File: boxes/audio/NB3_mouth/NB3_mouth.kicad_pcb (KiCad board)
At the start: 2 copper layers, 20 x 18 mm, 4 parts, among them IC1 MAX98357AETE+T, J1 Conn_02x03_Odd_Even, J2 Conn_02x03_Odd_Even

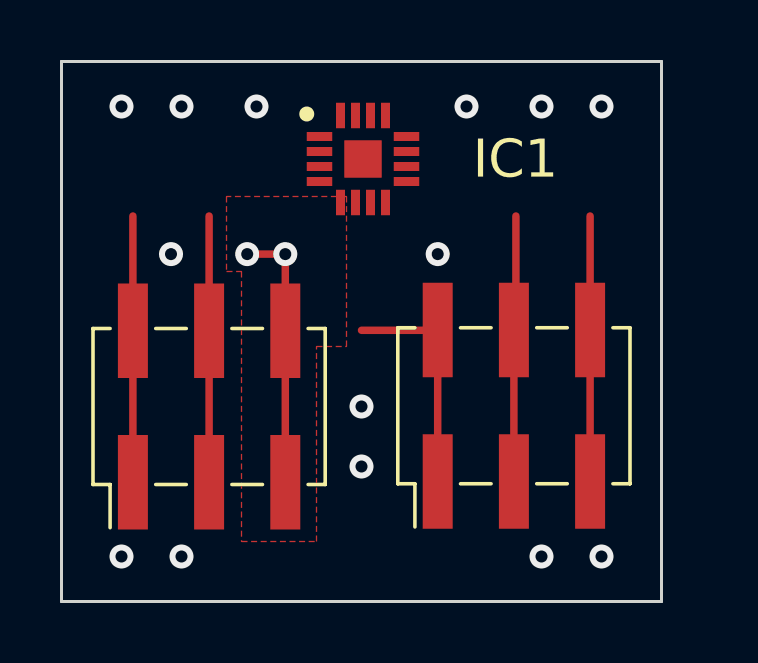
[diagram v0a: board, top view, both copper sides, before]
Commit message: Tweak NB3_mouth
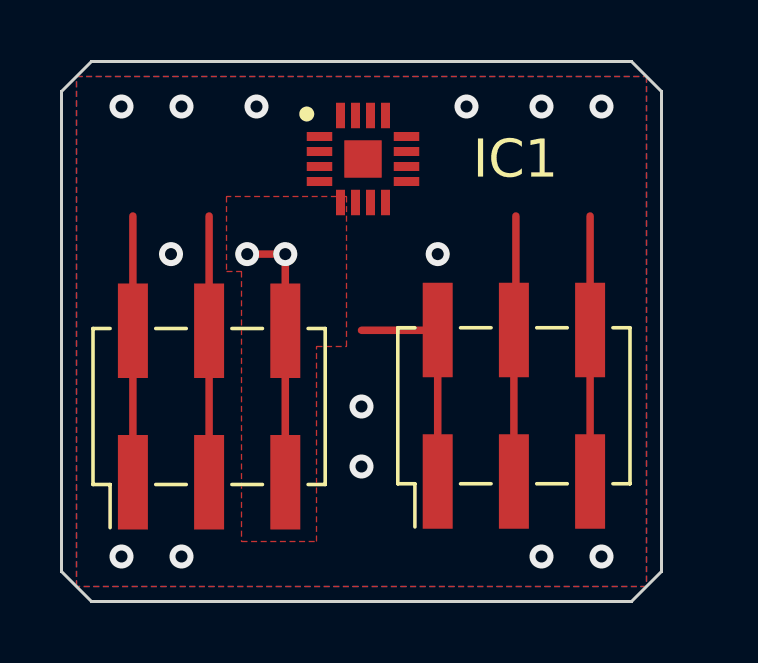
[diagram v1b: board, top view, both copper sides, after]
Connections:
- IC1 pad 11: unconnected-(IC1-GND_2-Pad11) -> GND
- IC1 pad 3: unconnected-(IC1-GND_1-Pad3) -> GND
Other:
- outline, holes or cut-outs redrawn
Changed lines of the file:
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@@
   (net 6 "/LR")
   (net 7 "unconnected-(IC1-GAIN_SLOT-Pad2)")
-  (net 8 "unconnected-(IC1-GND_1-Pad3)")
-  (net 9 "unconnected-(IC1-~{SD_MODE}-Pad4)")
-  (net 10 "unconnected-(IC1-N.C._1-Pad5)")
-  (net 11 "unconnected-(IC1-N.C._2-Pad6)")
-  (net 12 "unconnected-(IC1-VDD_1-Pad7)")
-  (net 13 "unconnected-(IC1-VDD_2-Pad8)")
-  (net 14 "unconnected-(IC1-OUTP-Pad9)")
-  (net 15 "unconnected-(IC1-OUTN-Pad10)")
-  (net 16 "unconnected-(IC1-GND_2-Pad11)")
-  (net 17 "unconnected-(IC1-N.C._3-Pad12)")
-  (net 18 "unconnected-(IC1-N.C._4-Pad13)")
-  (net 19 "unconnected-(IC1-LRCLK-Pad14)")
-  (net 20 "unconnected-(IC1-GND_3-Pad15)")
-  (net 21 "unconnected-(IC1-BCLK-Pad16)")
-  (net 22 "unconnected-(IC1-THERMAL_PAD-Pad17)")
-  (net 23 "+5V")
+  (net 8 "unconnected-(IC1-~{SD_MODE}-Pad4)")
+  (net 9 "unconnected-(IC1-N.C._1-Pad5)")
+  (net 10 "unconnected-(IC1-N.C._2-Pad6)")
+  (net 11 "unconnected-(IC1-VDD_1-Pad7)")
+  (net 12 "unconnected-(IC1-VDD_2-Pad8)")
+  (net 13 "unconnected-(IC1-OUTP-Pad9)")
+  (net 14 "unconnected-(IC1-OUTN-Pad10)")
+  (net 15 "unconnected-(IC1-N.C._3-Pad12)")
+  (net 16 "unconnected-(IC1-N.C._4-Pad13)")
+  (net 17 "unconnected-(IC1-LRCLK-Pad14)")
+  (net 18 "unconnected-(IC1-GND_3-Pad15)")
+  (net 19 "unconnected-(IC1-BCLK-Pad16)")
+  (net 20 "unconnected-(IC1-THERMAL_PAD-Pad17)")
+  (net 21 "+5V")
   (footprint "NB3_mouth:I2S_DAC-AMP_MAX98357A" (layer "F.Cu")
     (at 151.13 101.525)
@@
       (net 7 "unconnected-(IC1-GAIN_SLOT-Pad2)") (pinfunction "GAIN_SLOT") (pintype "passive"))
     (pad "3" smd rect (at -1.45 0.25 90) (size 0.3 0.85) (layers "F.Cu" "F.Paste" "F.Mask")
-      (net 8 "unconnected-(IC1-GND_1-Pad3)") (pinfunction "GND_1") (pintype "passive"))
+      (net 2 "GND") (pinfunction "GND_1") (pintype "passive"))
     (pad "4" smd rect (at -1.45 0.75 90) (size 0.3 0.85) (layers "F.Cu" "F.Paste" "F.Mask")
-      (net 9 "unconnected-(IC1-~{SD_MODE}-Pad4)") (pinfunction "~{SD_MODE}") (pintype "passive"))
+      (net 8 "unconnected-(IC1-~{SD_MODE}-Pad4)") (pinfunction "~{SD_MODE}") (pintype "passive"))
     (pad "5" smd rect (at -0.75 1.45) (size 0.3 0.85) (layers "F.Cu" "F.Paste" "F.Mask")
-      (net 10 "unconnected-(IC1-N.C._1-Pad5)") (pinfunction "N.C._1") (pintype "passive"))
+      (net 9 "unconnected-(IC1-N.C._1-Pad5)") (pinfunction "N.C._1") (pintype "passive"))
     (pad "6" smd rect (at -0.25 1.45) (size 0.3 0.85) (layers "F.Cu" "F.Paste" "F.Mask")
-      (net 11 "unconnected-(IC1-N.C._2-Pad6)") (pinfunction "N.C._2") (pintype "passive"))
+      (net 10 "unconnected-(IC1-N.C._2-Pad6)") (pinfunction "N.C._2") (pintype "passive"))
     (pad "7" smd rect (at 0.25 1.45) (size 0.3 0.85) (layers "F.Cu" "F.Paste" "F.Mask")
-      (net 12 "unconnected-(IC1-VDD_1-Pad7)") (pinfunction "VDD_1") (pintype "passive"))
+      (net 11 "unconnected-(IC1-VDD_1-Pad7)") (pinfunction "VDD_1") (pintype "passive"))
     (pad "8" smd rect (at 0.75 1.45) (size 0.3 0.85) (layers "F.Cu" "F.Paste" "F.Mask")
-      (net 13 "unconnected-(IC1-VDD_2-Pad8)") (pinfunction "VDD_2") (pintype "passive"))
+      (net 12 "unconnected-(IC1-VDD_2-Pad8)") (pinfunction "VDD_2") (pintype "passive"))
     (pad "9" smd rect (at 1.45 0.75 90) (size 0.3 0.85) (layers "F.Cu" "F.Paste" "F.Mask")
-      (net 14 "unconnected-(IC1-OUTP-Pad9)") (pinfunction "OUTP") (pintype "passive"))
+      (net 13 "unconnected-(IC1-OUTP-Pad9)") (pinfunction "OUTP") (pintype "passive"))
     (pad "10" smd rect (at 1.45 0.25 90) (size 0.3 0.85) (layers "F.Cu" "F.Paste" "F.Mask")
-      (net 15 "unconnected-(IC1-OUTN-Pad10)") (pinfunction "OUTN") (pintype "passive"))
+      (net 14 "unconnected-(IC1-OUTN-Pad10)") (pinfunction "OUTN") (pintype "passive"))
     (pad "11" smd rect (at 1.45 -0.25 90) (size 0.3 0.85) (layers "F.Cu" "F.Paste" "F.Mask")
-      (net 16 "unconnected-(IC1-GND_2-Pad11)") (pinfunction "GND_2") (pintype "passive"))
+      (net 2 "GND") (pinfunction "GND_2") (pintype "passive"))
     (pad "12" smd rect (at 1.45 -0.75 90) (size 0.3 0.85) (layers "F.Cu" "F.Paste" "F.Mask")
-      (net 17 "unconnected-(IC1-N.C._3-Pad12)") (pinfunction "N.C._3") (pintype "passive"))
+      (net 15 "unconnected-(IC1-N.C._3-Pad12)") (pinfunction "N.C._3") (pintype "passive"))
     (pad "13" smd rect (at 0.75 -1.45) (size 0.3 0.85) (layers "F.Cu" "F.Paste" "F.Mask")
-      (net 18 "unconnected-(IC1-N.C._4-Pad13)") (pinfunction "N.C._4") (pintype "passive"))
+      (net 16 "unconnected-(IC1-N.C._4-Pad13)") (pinfunction "N.C._4") (pintype "passive"))
     (pad "14" smd rect (at 0.25 -1.45) (size 0.3 0.85) (layers "F.Cu" "F.Paste" "F.Mask")
-      (net 19 "unconnected-(IC1-LRCLK-Pad14)") (pinfunction "LRCLK") (pintype "passive"))
+      (net 17 "unconnected-(IC1-LRCLK-Pad14)") (pinfunction "LRCLK") (pintype "passive"))
     (pad "15" smd rect (at -0.25 -1.45) (size 0.3 0.85) (layers "F.Cu" "F.Paste" "F.Mask")
-      (net 20 "unconnected-(IC1-GND_3-Pad15)") (pinfunction "GND_3") (pintype "passive"))
+      (net 18 "unconnected-(IC1-GND_3-Pad15)") (pinfunction "GND_3") (pintype "passive"))
     (pad "16" smd rect (at -0.75 -1.45) (size 0.3 0.85) (layers "F.Cu" "F.Paste" "F.Mask")
-      (net 21 "unconnected-(IC1-BCLK-Pad16)") (pinfunction "BCLK") (pintype "passive"))
+      (net 19 "unconnected-(IC1-BCLK-Pad16)") (pinfunction "BCLK") (pintype "passive"))
     (pad "17" smd rect (at 0 0) (size 1.25 1.25) (layers "F.Cu" "F.Paste" "F.Mask")
-      (net 22 "unconnected-(IC1-THERMAL_PAD-Pad17)") (pinfunction "THERMAL_PAD") (pintype "passive"))
+      (net 20 "unconnected-(IC1-THERMAL_PAD-Pad17)") (pinfunction "THERMAL_PAD") (pintype "passive"))
     (model "${KIPRJMOD}/libraries/parts/I2S_DAC-AMP_MAX98357A/I2S_DAC-AMP_MAX98357A.step"
       (opacity 0.4400)      (offset (xyz 0 0 0))
@@
       (net 3 "/SCK") (pinfunction "Pin_2") (pintype "passive"))
     (pad "3" smd rect (at -2.525 0 90) (size 3.15 1) (layers "F.Cu" "F.Paste" "F.Mask")
-      (net 23 "+5V") (pinfunction "Pin_3") (pintype "passive"))
+      (net 21 "+5V") (pinfunction "Pin_3") (pintype "passive"))
     (pad "4" smd rect (at 2.525 0 90) (size 3.15 1) (layers "F.Cu" "F.Paste" "F.Mask")
-      (net 23 "+5V") (pinfunction "Pin_4") (pintype "passive"))
+      (net 21 "+5V") (pinfunction "Pin_4") (pintype "passive"))
     (pad "5" smd rect (at -2.525 2.54 90) (size 3.15 1) (layers "F.Cu" "F.Paste" "F.Mask")
       (net 2 "GND") (pinfunction "Pin_5") (pintype "passive"))
@@
   (gr_line (start 147.08 102.775) (end 145.58 102.775)
     (stroke (width 0.15) (type default)) (layer "B.SilkS"))
-  (gr_rect (start 141.08 98.275) (end 161.08 116.275)
-    (stroke (width 0.1) (type solid)) (fill none) (layer "Edge.Cuts"))
+  (gr_line (start 161.08 99.275) (end 161.08 115.275)
+    (stroke (width 0.1) (type default)) (layer "Edge.Cuts"))
+  (gr_line (start 161.08 115.275) (end 160.08 116.275)
+    (stroke (width 0.1) (type default)) (layer "Edge.Cuts"))
+  (gr_line (start 141.08 99.275) (end 142.08 98.275)
+    (stroke (width 0.1) (type default)) (layer "Edge.Cuts"))
+  (gr_line (start 142.08 116.275) (end 141.08 115.275)
+    (stroke (width 0.1) (type default)) (layer "Edge.Cuts"))
+  (gr_line (start 141.08 115.275) (end 141.08 99.275)
+    (stroke (width 0.1) (type default)) (layer "Edge.Cuts"))
+  (gr_line (start 142.08 98.275) (end 160.08 98.275)
+    (stroke (width 0.1) (type default)) (layer "Edge.Cuts"))
+  (gr_line (start 160.08 98.275) (end 161.08 99.275)
+    (stroke (width 0.1) (type default)) (layer "Edge.Cuts"))
+  (gr_line (start 160.08 116.275) (end 142.08 116.275)
+    (stroke (width 0.1) (type default)) (layer "Edge.Cuts"))
   (gr_text "SCK" (at 143.46 112.465) (layer "B.SilkS")
     (effects (font (size 0.8 0.7) (thickness 0.15)) (justify mirror))
@@
   (segment (start 158.7 112.275) (end 158.7 107.225) (width 0.25) (layer "F.Cu") (net 6))
   (segment (start 158.7 107.225) (end 158.7 103.425) (width 0.25) (layer "F.Cu") (net 6))
-  (segment (start 146 103.425) (end 146 107.25) (width 0.25) (layer "F.Cu") (net 23))
-  (segment (start 146 112.3) (end 146 107.25) (width 0.25) (layer "F.Cu") (net 23))
+  (segment (start 146 103.425) (end 146 107.25) (width 0.25) (layer "F.Cu") (net 21))
+  (segment (start 146 112.3) (end 146 107.25) (width 0.25) (layer "F.Cu") (net 21))
   (zone (net 2) (net_name "GND") (layer "F.Cu") (hatch edge 0.508)
     (connect_pads (clearance 0.25))
@@
     (polygon
       (pts
-        (xy 141.08 98.275)
-        (xy 161.08 98.275)
-        (xy 161.08 116.275)
-        (xy 141.08 116.275)
+        (xy 141.58 98.775)
+        (xy 160.58 98.775)
+        (xy 160.58 115.775)
+        (xy 141.58 115.775)
       )
     )
@@
     (polygon
       (pts
-        (xy 161.08 116.275)
-        (xy 141.08 116.275)
-        (xy 141.08 98.275)
-        (xy 161.08 98.275)
+        (xy 160.58 115.775)
+        (xy 141.58 115.775)
+        (xy 141.58 98.775)
+        (xy 160.58 98.775)
       )
     )

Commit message: Add JST connector to NB3_mouth
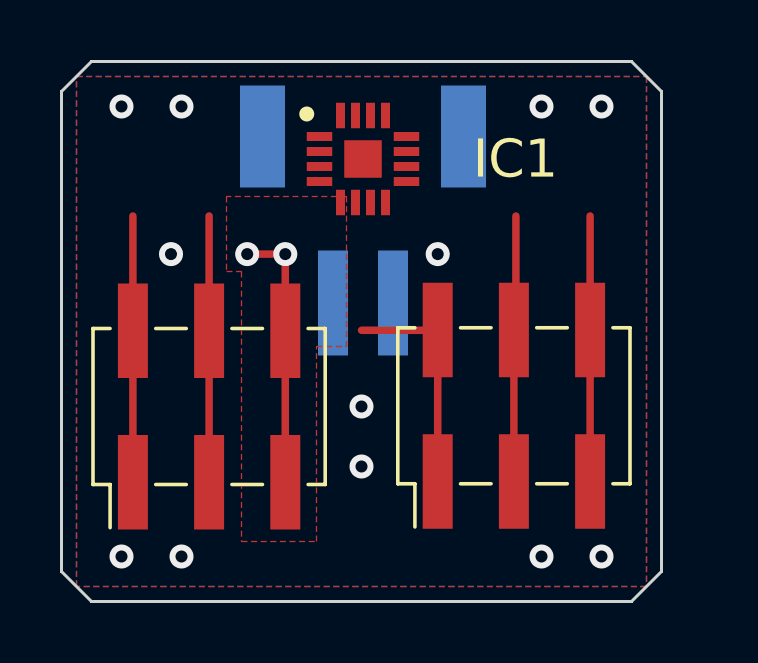
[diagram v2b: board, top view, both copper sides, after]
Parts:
- added J3: JST-PH2, NB3_mouth:Connector_Female_JST-PH2, B.Cu at (151.1, 106.3)
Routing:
- net GND: vias 16 -> 14
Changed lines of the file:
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@@
   (net 20 "unconnected-(IC1-THERMAL_PAD-Pad17)")
   (net 21 "+5V")
+  (net 22 "unconnected-(J3-Pad1)")
+  (net 23 "unconnected-(J3-Pad2)")
   (footprint "NB3_mouth:I2S_DAC-AMP_MAX98357A" (layer "F.Cu")
     (at 151.13 101.525)
@@
       (scale (xyz 1 1 1))
       (rotate (xyz 0 0 0))
+    )
+  )
+  (footprint "NB3_mouth:Connector_Female_JST-PH2" (layer "B.Cu")
+    (at 151.13 106.325)
+    (descr "JST-PH2")
+    (tags "Connector")
+    (property "Height" "")
+    (property "Manufacturer_Name" "Adafruit")
+    (property "Manufacturer_Part_Number" "1769")
+    (property "Mouser Part Number" "485-1769")
+    (property "Mouser Price/Stock" "https://www.mouser.co.uk/ProductDetail/Adafruit/1769?qs=GURawfaeGuBbgoGtf2XstA%3D%3D")
+    (property "Sheetfile" "NB3_mouth.kicad_sch")
+    (property "Sheetname" "")
+    (property "ki_description" " JST-PH 2-pin SMT Right Angle Connect")
+    (attr smd)
+    (fp_text reference "J3" (at -0.662 -3.794) (layer "B.SilkS")
+        (effects (font (size 1.27 1.27) (thickness 0.254)) (justify mirror))
+    )
+    (fp_text value " JST-PH2" (at 0 -8.6868) (layer "B.SilkS") hide
+        (effects (font (size 1.27 1.27) (thickness 0.254)) (justify mirror))
+    )
+    (fp_text user "${REFERENCE}" (at 0 3.6576) (layer "B.Fab")
+        (effects (font (size 1.27 1.27) (thickness 0.254)) (justify mirror))
+    )
+    (fp_line (start -3.95 0) (end -3.95 -3.425)
+      (stroke (width 0.2) (type solid)) (layer "B.SilkS"))
+    (fp_line (start -3.95 0) (end -1.9 0)
+      (stroke (width 0.2) (type solid)) (layer "B.SilkS"))
+    (fp_line (start -2.196 -6.849) (end 2.196 -6.849)
+      (stroke (width 0.2) (type solid)) (layer "B.SilkS"))
+    (fp_line (start 3.95 0) (end 1.9 0)
+      (stroke (width 0.2) (type solid)) (layer "B.SilkS"))
+    (fp_line (start 3.95 0) (end 3.95 -3.425)
+      (stroke (width 0.2) (type solid)) (layer "B.SilkS"))
+    (fp_circle (center -1.069 2.582) (end -1.069 2.53)
+      (stroke (width 0.2) (type solid)) (fill none) (layer "B.SilkS"))
+    (fp_line (start -3.95 -6.849) (end -3.95 0)
+      (stroke (width 0.2) (type solid)) (layer "B.Fab"))
+    (fp_line (start -3.95 0) (end 3.95 0)
+      (stroke (width 0.2) (type solid)) (layer "B.Fab"))
+    (fp_line (start 3.95 -6.849) (end -3.95 -6.849)
+      (stroke (width 0.2) (type solid)) (layer "B.Fab"))
+    (fp_line (start 3.95 0) (end 3.95 -6.849)
+      (stroke (width 0.2) (type solid)) (layer "B.Fab"))
+    (pad "1" smd rect (at -1 0) (size 1 3.5) (layers "B.Cu" "B.Paste" "B.Mask")
+      (net 22 "unconnected-(J3-Pad1)") (pinfunction "1") (pintype "passive"))
+    (pad "2" smd rect (at 1 0) (size 1 3.5) (layers "B.Cu" "B.Paste" "B.Mask")
+      (net 23 "unconnected-(J3-Pad2)") (pinfunction "2") (pintype "passive"))
+    (pad "3" smd rect (at -3.35 -5.55) (size 1.5 3.4) (layers "B.Cu" "B.Paste" "B.Mask"))
+    (pad "4" smd rect (at 3.35 -5.55) (size 1.5 3.4) (layers "B.Cu" "B.Paste" "B.Mask"))
+    (model "${KIPRJMOD}/libraries/parts/Connector_Female_JST-PH2/Connector_Female_JST-PH2.stp"
+      (offset (xyz 0 -7 0))
+      (scale (xyz 1 1 1))
+      (rotate (xyz -90 0 0))
     )
   )
@@
   (via (at 144.73 104.695) (size 0.8) (drill 0.4) (layers "F.Cu" "B.Cu") (free) (net 2))
   (via (at 147.27 104.695) (size 0.8) (drill 0.4) (layers "F.Cu" "B.Cu") (net 2))
-  (via (at 147.58 99.775) (size 0.8) (drill 0.4) (layers "F.Cu" "B.Cu") (net 2))
-  (via (at 154.58 99.775) (size 0.8) (drill 0.4) (layers "F.Cu" "B.Cu") (net 2))
   (segment (start 143.46 103.425) (end 143.46 107.25) (width 0.25) (layer "F.Cu") (net 3))
   (segment (start 143.46 112.3) (end 143.46 107.25) (width 0.25) (layer "F.Cu") (net 3))

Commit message: Upload NB3_ear "fab" v2
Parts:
- added R1: R, Resistor_SMD:R_0402_1005Metric, F.Cu at (158.3, 101.0)
- added R2: R, Resistor_SMD:R_0402_1005Metric, F.Cu at (158.3, 103.0)
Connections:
- IC1 pad 1: unconnected-(IC1-DIN-Pad1) -> /SD
- IC1 pad 10: unconnected-(IC1-OUTN-Pad10) -> /Speaker-
- IC1 pad 14: unconnected-(IC1-LRCLK-Pad14) -> /WS
- IC1 pad 15: unconnected-(IC1-GND_3-Pad15) -> GND
- IC1 pad 16: unconnected-(IC1-BCLK-Pad16) -> /SCK
- IC1 pad 17: unconnected-(IC1-THERMAL_PAD-Pad17) -> GND
- IC1 pad 2: unconnected-(IC1-GAIN_SLOT-Pad2) -> /Gain
- IC1 pad 4: unconnected-(IC1-~{SD_MODE}-Pad4) -> Net-(IC1-~{SD_MODE})
- IC1 pad 7: unconnected-(IC1-VDD_1-Pad7) -> +5V
- IC1 pad 8: unconnected-(IC1-VDD_2-Pad8) -> +5V
- IC1 pad 9: unconnected-(IC1-OUTP-Pad9) -> /Speaker+
- J2 pad 5: /LR -> /Gain
- J2 pad 6: /LR -> /Gain
- J3 pad 1: unconnected-(J3-Pad1) -> /Speaker+
- J3 pad 2: unconnected-(J3-Pad2) -> /Speaker-
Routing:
- net /LR: track 8.85 -> 0.00 mm
- net /Gain: track 0.00 -> 5.05 mm
- net /WS: track 8.88 -> 5.05 mm
- net /SCK: track 8.88 -> 5.05 mm
- net +5V: track 8.88 -> 5.05 mm
- net GND: track 8.87 -> 5.05 mm, vias 14 -> 9
- net /SD: track 7.59 -> 5.06 mm

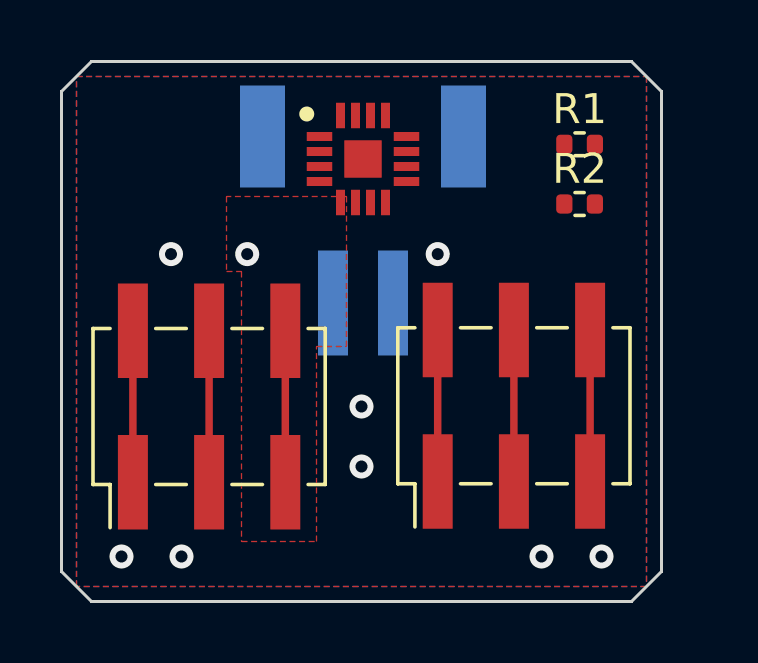
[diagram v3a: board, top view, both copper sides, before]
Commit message: Ref 1 of NB3 Mouth
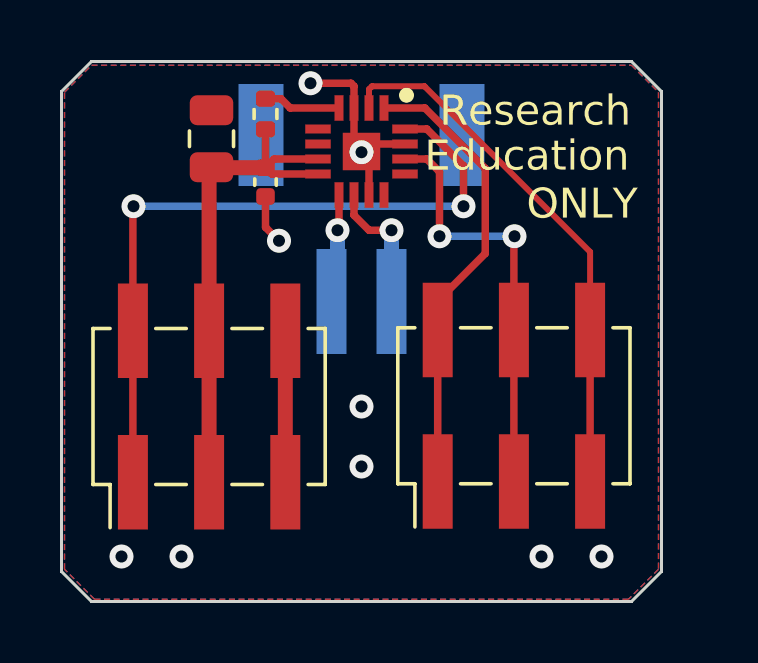
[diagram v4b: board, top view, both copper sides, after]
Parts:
- removed R2: R, Resistor_SMD:R_0402_1005Metric
- added C1: 10uF, Capacitor_SMD:C_0805_2012Metric, F.Cu at (146.1, 100.8)
- added C2: 0.1uF, Capacitor_SMD:C_0402_1005Metric, F.Cu at (147.9, 102.3)
- G***: footprint NB3_ear:Logo_VK_5mm -> NB3_mouth:Logo_VK_5mm
- R1: value R -> 1M
- moved R1 10.5 mm to (147.9, 100.0), turned to 90 degrees
- moved G*** 9.31 mm to (158.2, 101.2)
- moved IC1 0.25 mm to (151.1, 101.3), turned to -90 degrees
- moved J3 0.07 mm to (151.1, 106.3)
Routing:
- net /SCK: track 5.05 -> 24.0 mm, vias 0 -> 2
- net /Gain: track 5.05 -> 18.0 mm
- net +5V: track 5.05 -> 17.3 mm
- net /SD: track 5.06 -> 15.3 mm
- net /WS: track 5.05 -> 14.2 mm, vias 0 -> 2
- net GND: track 5.05 -> 13.6 mm
- net /Speaker-: track 0.00 -> 4.51 mm, vias 0 -> 1
- net /Speaker+: track 0.00 -> 3.65 mm, vias 0 -> 1
- net Net-(IC1-~{SD_MODE}): track 0.00 -> 2.58 mm
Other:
- board text added: "5V"
- board text added: "Education"
- board text added: "GN"
- board text added: "ONLY"
- board text added: "Research"
- board text removed: "3v3"
- board text removed: "LR"
